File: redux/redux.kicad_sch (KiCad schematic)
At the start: 250 parts, among them J11 DNP, J12 DNP, J13 DNP, J14 Backplane, J3 Common, J4 Ext-2, J5 Ext-1, J6 Master, J7 Ext+1, J8 Ext+2, M1000 Bracket, Q1 MMBT3906, U1 MC100LVEL16, U13 MC100LVEL14, U15 SY89421V, U16 LM311, U34 AD7841, U44 AD586, U45 AD586, U62 LT1086-ADJ, U63 LT1086-ADJ, U64 16715-89002, U65 74CBT3125, U66 SG-615P 19.6608MHz, U67 SN74FB2040, U68 MC100LVEL11, U73 MC100LVEL16, U74 MC10EL34, U75 PCF8584, U76 74ABT540, U79 NEL HS-2810 101MHz

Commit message: redux work
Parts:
- removed J11, J12, J13: DNP, fp:PinHeader_2x10_P2.54mm_Vertical, symbol Connector_Generic:Conn_02x10_Odd_Even
- removed R1, R2, R3, R4, R5, R6, R7, R8: 100, fp:R_Array_Convex_4x0603, symbol Device:R_Pack04
- removed R1038, R1044: DNP, fp:R0805, symbol Device:R_Small
- removed R1040, R1047, R1053, R1054, R1057, R1231, R1232, R1235, R1238, R1241: 31.6, fp:R0805, symbol Device:R_Small
- removed R1242, R1243: 147, fp:R0805, symbol Device:R_Small
- removed RP11: 150, fp:SOIC-16W_5.3x10.2mm_P1.27mm, symbol 16717a:RPack8
- added C2: 1.1n, fp:C0805, symbol Device:C_Small
- added R13, R14: 150, fp:R_Array_Convex_4x0603, symbol Device:R_Pack04
- added R170, R171, R180, R181, R190, R191: 100, fp:SOIC-16W_5.3x10.2mm_P1.27mm, symbol 16717a:RPack8
- R10, R11, R9: value 100 -> 31.6
- R12: value 100 -> 150
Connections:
- net +1.5V: now also R170.10, R170.11, R170.12, R170.13, R170.14, R170.15, R170.16, R170.9, R171.1, R171.2, R171.3, R171.4, R171.5, R171.6, R171.7, R171.8, R180.10, R180.11, R180.12, R180.13, R180.14, R180.15, R180.16, R180.9, R181.1, R181.2, R181.3, R181.4, R181.5, R181.6, R181.7, R181.8, R190.10, R190.11, R190.12, R190.13, R190.14, R190.15, R190.16, R190.9, R191.1, R191.2, R191.3, R191.4, R191.5, R191.6, R191.7, R191.8; no longer R10.1 (R1.1), R10.2 (R2.1), R10.3 (R3.1), R10.4 (R4.1), R11.1 (R1.1), R11.2 (R2.1), R11.3 (R3.1), R11.4 (R4.1), R12.1 (R1.1), R12.2 (R2.1), R12.3 (R3.1), R12.4 (R4.1), R9.1 (R1.1), R9.2 (R2.1), R9.3 (R3.1), R9.4 (R4.1)
- net +3.3VP: now also C2.2
- net -5.2V: now also R12.5 (R4.2), R12.6 (R3.2), R12.7 (R2.2), R12.8 (R1.2), R13.5 (R4.2), R13.6 (R3.2), R13.7 (R2.2), R13.8 (R1.2), R14.5 (R4.2), R14.6 (R3.2), R14.7 (R2.2), R14.8 (R1.2)
- net BA_{0}: now also R191.9
- net BA_{10}: now also R181.11
- net BA_{11}: now also R181.12
- net BA_{12}: now also R181.13
- net BA_{13}: now also R181.14
- net BA_{14}: now also R181.15
- net BA_{15}: now also R181.16
- net BA_{16}: now also R171.9
- net BA_{17}: now also R171.10
- net BA_{18}: now also R171.11
- net BA_{19}: now also R171.12
- net BA_{1}: now also R191.10
- net BA_{20}: now also R171.13
- net BA_{21}: now also R171.14
- net BA_{22}: now also R171.15
- net BA_{23}: now also R171.16
- net BA_{2}: now also R191.11
- net BA_{3}: now also R191.12
- net BA_{4}: now also R191.13
- net BA_{5}: now also R191.14
- net BA_{6}: now also R191.15
- net BA_{7}: now also R191.16
- net BA_{8}: now also R181.9
- net BA_{9}: now also R181.10
- net BB_{0}: now also R190.8; no longer R12.5 (R4.2)
- net BB_{10}: now also R180.6; no longer R10.7 (R2.2)
- net BB_{11}: now also R180.5; no longer R10.8 (R1.2)
- net BB_{12}: now also R180.4; no longer R9.5 (R4.2)
- net BB_{13}: now also R180.3; no longer R9.6 (R3.2)
- net BB_{14}: now also R180.2; no longer R9.7 (R2.2)
- net BB_{15}: now also R180.1; no longer R9.8 (R1.2)
- net BB_{16}: now also R170.8
- net BB_{17}: now also R170.7
- net BB_{18}: now also R170.6
- net BB_{19}: now also R170.5
- net BB_{1}: now also R190.7; no longer R12.6 (R3.2)
- net BB_{20}: now also R170.4
- net BB_{21}: now also R170.3
- net BB_{22}: now also R170.2
- net BB_{23}: now also R170.1
- net BB_{2}: now also R190.6; no longer R12.7 (R2.2)
- net BB_{3}: now also R190.5; no longer R12.8 (R1.2)
- net BB_{4}: now also R190.4; no longer R11.5 (R4.2)
- net BB_{5}: now also R190.3; no longer R11.6 (R3.2)
- net BB_{6}: now also R190.2; no longer R11.7 (R2.2)
- net BB_{7}: now also R190.1; no longer R11.8 (R1.2)
- net BB_{8}: now also R180.8; no longer R10.5 (R4.2)
- net BB_{9}: now also R180.7; no longer R10.6 (R3.2)
- net GND: now also R11.7 (R2.2), R11.8 (R1.2), C2.1
- net TEST_CLK_{L0}: now also R9.6 (R3.2)
- net TEST_CLK_{L1}: now also R9.8 (R1.2)
- net TEST_CLK_{L2}: now also R10.6 (R3.2)
- net TEST_CLK_{L3}: now also R10.8 (R1.2)
- net TEST_CLK_{L4}: now also R11.6 (R3.2)
- net TEST_CLK_{R0}: now also R9.5 (R4.2)
- net TEST_CLK_{R1}: now also R9.7 (R2.2)
- net TEST_CLK_{R2}: now also R10.5 (R4.2)
- net TEST_CLK_{R3}: now also R10.7 (R2.2)
- net TEST_CLK_{R4}: now also R11.5 (R4.2)
- net at U13.3 (OUT_{1}): now also R12.2 (R2.1), R9.1 (R1.1), R9.2 (R2.1)
- net at U13.1 (OUT_{0}): now also R12.4 (R4.1), R9.3 (R3.1), R9.4 (R4.1)
- net at U13.9 (OUT_{4}): now also R11.3 (R3.1), R11.4 (R4.1), R14.4 (R4.1)
- net at U13.5 (OUT_{2}): now also R10.3 (R3.1), R10.4 (R4.1), R13.4 (R4.1)
- net at U13.7 (OUT_{3}): now also R10.1 (R1.1), R10.2 (R2.1), R13.2 (R2.1)
- net at U13.6 (~{OUT_{2}}): now also R13.3 (R3.1)
- net at U13.4 (~{OUT_{1}}): now also R12.1 (R1.1)
- net at U13.2 (~{OUT_{0}}): now also R12.3 (R3.1)
- net at U13.8 (~{OUT_{3}}): now also R13.1 (R1.1)
- net at U13.10 (~{OUT_{4}}): now also R14.3 (R3.1)
- net SYS_CLK renamed SYS_CLK+
- net SYS_CLK_{LEFT} renamed SYS_CLK_{LEFT}+
- net SYS_CLK_{RIGHT} renamed SYS_CLK_{RIGHT}+
- net ~{SYS_CLK_{LEFT}} renamed SYS_CLK_{LEFT}-
- net ~{SYS_CLK_{RIGHT}} renamed SYS_CLK_{RIGHT}-
- net ~{SYS_CLK} renamed SYS_CLK-
- no-connect marks 41 -> 34

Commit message: replace SOIC resistor arrays
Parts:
- removed R213: 51, fp:SOIC-16W_5.3x10.2mm_P1.27mm, symbol 16717a:RPack8
- removed RP10, RP16, RP4, RP5, RP6, RP7, RP8, RP9: 33, fp:SOIC-16W_5.3x10.2mm_P1.27mm, symbol 16717a:RPack8
- removed RP17, RP18: 100, fp:SOIC-16W_5.3x10.2mm_P1.27mm, symbol 16717a:RPack8
- removed RP3: 1k, fp:SOIC-16W_5.3x10.2mm_P1.27mm, symbol 16717a:R_Network15
- added R15, R16, R17: 1k, fp:R_Array_Convex_4x0603, symbol Device:R_Pack04
- added R18, R19, R20, R21, R22, R23, R24, R25, R26, R27, R28, R29, R34, R35, R36, R37: 33, fp:R_Array_Convex_4x0603, symbol Device:R_Pack04
- added R30, R31, R38, R39: 100, fp:R_Array_Convex_4x0603, symbol Device:R_Pack04
- added R32, R33: 51, fp:R_Array_Convex_4x0603, symbol Device:R_Pack04
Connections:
- net +2.5V: now also R38.5 (R4.2), R38.6 (R3.2), R38.7 (R2.2), R38.8 (R1.2), R39.5 (R4.2), R39.6 (R3.2), R39.7 (R2.2), R39.8 (R1.2)
- net +3.3V: now also R15.1 (R1.1), R15.2 (R2.1), R15.3 (R3.1), R15.4 (R4.1), R16.1 (R1.1), R16.2 (R2.1), R16.3 (R3.1), R16.4 (R4.1), R17.1 (R1.1), R17.2 (R2.1), R17.3 (R3.1), R17.4 (R4.1), R30.5 (R4.2), R30.6 (R3.2), R30.7 (R2.2), R30.8 (R1.2), R31.5 (R4.2), R31.6 (R3.2), R31.7 (R2.2), R31.8 (R1.2)
- net CTRL0L: now also R31.1 (R1.1)
- net CTRL0R: now also R30.1 (R1.1)
- net CTRL10L: now also R28.4 (R4.1)
- net CTRL10R: now also R28.3 (R3.1)
- net CTRL1L: now also R31.2 (R2.1)
- net CTRL1R: now also R30.2 (R2.1)
- net CTRL2L: now also R31.3 (R3.1)
- net CTRL2R: now also R30.3 (R3.1)
- net CTRL3L: now also R31.4 (R4.1)
- net CTRL3R: now also R30.4 (R4.1)
- net CTRL6L: now also R29.2 (R2.1)
- net CTRL6R: now also R29.1 (R1.1)
- net CTRL7L: now also R29.4 (R4.1)
- net CTRL7R: now also R29.3 (R3.1)
- net CTRL9L: now also R28.2 (R2.1)
- net CTRL9R: now also R28.1 (R1.1)
- net SYS_CLK+: now also R32.4 (R4.1)
- net SYS_CLK-: now also R32.2 (R2.1)
- net SYS_CLK_{LEFT}+: now also R33.4 (R4.1)
- net SYS_CLK_{LEFT}-: now also R33.2 (R2.1)
- net SYS_CLK_{RIGHT}+: now also R33.3 (R3.1)
- net SYS_CLK_{RIGHT}-: now also R33.1 (R1.1)
- net ZCTRL0: now also R16.8 (R1.2)
- net ZCTRL1: now also R16.7 (R2.2)
- net ZCTRL2: now also R16.6 (R3.2)
- net ZCTRL3: now also R15.6 (R3.2)
- net ZCTRL4: now also R15.8 (R1.2)
- net ZCTRL5: now also R15.7 (R2.2)
- net ZCTRL6: now also R15.5 (R4.2)
- net ~{BIFE_{0}}: now also R38.1 (R1.1)
- net ~{BIFE_{1}}: now also R38.2 (R2.1)
- net ~{BIFE_{2}}: now also R38.3 (R3.1)
- net ~{BIFE_{3}}: now also R38.4 (R4.1)
- net ~{BIFE_{4}}: now also R39.1 (R1.1)
- net ~{BIFE_{5}}: now also R39.2 (R2.1)
- net ~{BIFE_{6}}: now also R39.3 (R3.1)
- net ~{BIFE_{7}}: now also R39.4 (R4.1)
- net ~{EVENT_LEFT_{0}}: now also R36.7 (R2.2)
- net ~{EVENT_LEFT_{1}}: now also R36.5 (R4.2)
- net ~{EVENT_LEFT_{2}}: now also R37.7 (R2.2)
- net ~{EVENT_LEFT_{3}}: now also R37.5 (R4.2)
- net ~{EVENT_LEFT_{4}}: now also R34.7 (R2.2)
- net ~{EVENT_LEFT_{5}}: now also R34.5 (R4.2)
- net ~{EVENT_LEFT_{6}}: now also R35.7 (R2.2)
- net ~{EVENT_LEFT_{7}}: now also R35.5 (R4.2)
- net ~{EVENT_RIGHT_{0}}: now also R36.8 (R1.2)
- net ~{EVENT_RIGHT_{1}}: now also R36.6 (R3.2)
- net ~{EVENT_RIGHT_{2}}: now also R37.8 (R1.2)
- net ~{EVENT_RIGHT_{3}}: now also R37.6 (R3.2)
- net ~{EVENT_RIGHT_{4}}: now also R34.8 (R1.2)
- net ~{EVENT_RIGHT_{5}}: now also R34.6 (R3.2)
- net ~{EVENT_RIGHT_{6}}: now also R35.8 (R1.2)
- net ~{EVENT_RIGHT_{7}}: now also R35.6 (R3.2)
- net ~{MEM_CAS_{L0}}: now also R24.3 (R3.1)
- net ~{MEM_CAS_{L10}}: now also R23.2 (R2.1)
- net ~{MEM_CAS_{L11}}: now also R23.4 (R4.1)
- net ~{MEM_CAS_{L12}}: now also R25.3 (R3.1)
- net ~{MEM_CAS_{L13}}: now also R26.1 (R1.1)
- net ~{MEM_CAS_{L14}}: now also R23.3 (R3.1)
- net ~{MEM_CAS_{L15}}: now also R24.1 (R1.1)
- net ~{MEM_CAS_{L16}}: now also R26.2 (R2.1)
- net ~{MEM_CAS_{L1}}: now also R25.1 (R1.1)
- net ~{MEM_CAS_{L2}}: now also R22.3 (R3.1)
- net ~{MEM_CAS_{L3}}: now also R23.1 (R1.1)
- net ~{MEM_CAS_{L4}}: now also R24.2 (R2.1)
- net ~{MEM_CAS_{L5}}: now also R24.4 (R4.1)
- net ~{MEM_CAS_{L6}}: now also R22.2 (R2.1)
- net ~{MEM_CAS_{L7}}: now also R22.4 (R4.1)
- net ~{MEM_CAS_{L8}}: now also R25.2 (R2.1)
- net ~{MEM_CAS_{L9}}: now also R25.4 (R4.1)
- net ~{MEM_CAS_{R0}}: now also R20.2 (R2.1)
- net ~{MEM_CAS_{R10}}: now also R19.1 (R1.1)
- net ~{MEM_CAS_{R11}}: now also R19.3 (R3.1)
- net ~{MEM_CAS_{R12}}: now also R21.2 (R2.1)
- net ~{MEM_CAS_{R13}}: now also R21.4 (R4.1)
- net ~{MEM_CAS_{R14}}: now also R19.2 (R2.1)
- net ~{MEM_CAS_{R15}}: now also R19.4 (R4.1)
- net ~{MEM_CAS_{R16}}: now also R22.1 (R1.1)
- net ~{MEM_CAS_{R1}}: now also R20.4 (R4.1)
- net ~{MEM_CAS_{R2}}: now also R18.2 (R2.1)
- net ~{MEM_CAS_{R3}}: now also R18.4 (R4.1)
- net ~{MEM_CAS_{R4}}: now also R20.1 (R1.1)
- net ~{MEM_CAS_{R5}}: now also R20.3 (R3.1)
- net ~{MEM_CAS_{R6}}: now also R18.1 (R1.1)
- net ~{MEM_CAS_{R7}}: now also R18.3 (R3.1)
- net ~{MEM_CAS_{R8}}: now also R21.1 (R1.1)
- net ~{MEM_CAS_{R9}}: now also R21.3 (R3.1)
- net ~{ZCS_{0}}: now also R16.5 (R4.2), R26.3 (R3.1)
- net ~{ZCS_{1}}: now also R17.8 (R1.2), R26.4 (R4.1)
- net ~{ZCS_{2}}: now also R17.7 (R2.2), R27.1 (R1.1)
- net ~{ZCS_{3}}: now also R17.6 (R3.2), R27.2 (R2.1)
- net ~{ZCS_{4}}: now also R17.5 (R4.2), R27.3 (R3.1)
- net at C1124.1, R1119.1: now also R33.7 (R2.2), R33.8 (R1.2)
- net at U64.118 (~{ZCS_{4}}): now also R27.6 (R3.2)
- net at U64.117 (~{ZCS_{3}}): now also R27.7 (R2.2)
- net at U64.116 (~{ZCS_{2}}): now also R27.8 (R1.2)
- net at U64.115 (~{ZCS_{1}}): now also R26.5 (R4.2)
- net at U64.114 (~{ZCS_{0}}): now also R26.6 (R3.2)
- net at U64.102 (~{MEM_CAS_{L16}}): now also R26.7 (R2.2)
- net at U64.101 (~{MEM_CAS_{L13}}): now also R26.8 (R1.2)
- net at R1116.2, U68.1 (Y_{0}): now also R32.7 (R2.2)
- net at U64.100 (~{MEM_CAS_{L9}}): now also R25.5 (R4.2)
- net at U64.135 (CTRL9): now also R28.7 (R2.2), R28.8 (R1.2)
- net at U64.137 (CTRL10R): now also R28.6 (R3.2)
- net at U64.138 (CTRL10L): now also R28.5 (R4.2)
- net at U64.140 (CTRL6R): now also R29.8 (R1.2)
- net at U64.141 (CTRL6L): now also R29.7 (R2.2)
- net at U64.142 (CTRL7R): now also R29.6 (R3.2)
- net at U64.143 (CTRL7L): now also R29.5 (R4.2)
- net at U64.65 (~{MEM_CAS_{R6}}): now also R18.8 (R1.2)
- net at U64.66 (~{MEM_CAS_{R2}}): now also R18.7 (R2.2)
- net at U64.67 (~{MEM_CAS_{R7}}): now also R18.6 (R3.2)
- net at U64.68 (~{MEM_CAS_{R3}}): now also R18.5 (R4.2)
- net at U64.69 (~{MEM_CAS_{R10}}): now also R19.8 (R1.2)
- net at U64.70 (~{MEM_CAS_{R14}}): now also R19.7 (R2.2)
- net at U64.71 (~{MEM_CAS_{R11}}): now also R19.6 (R3.2)
- net at U64.72 (~{MEM_CAS_{R15}}): now also R19.5 (R4.2)
- net at U64.73 (~{MEM_CAS_{R4}}): now also R20.8 (R1.2)
- net at U64.74 (~{MEM_CAS_{R0}}): now also R20.7 (R2.2)
- net at U64.75 (~{MEM_CAS_{R5}}): now also R20.6 (R3.2)
- net at U64.76 (~{MEM_CAS_{R1}}): now also R20.5 (R4.2)
- net at U64.77 (~{MEM_CAS_{R8}}): now also R21.8 (R1.2)
- net at U64.81 (~{MEM_CAS_{R12}}): now also R21.7 (R2.2)
- net at U64.82 (~{MEM_CAS_{R9}}): now also R21.6 (R3.2)
- net at U64.83 (~{MEM_CAS_{R13}}): now also R21.5 (R4.2)
- net at U64.84 (~{MEM_CAS_{R16}}): now also R22.8 (R1.2)
- net at U64.85 (~{MEM_CAS_{L6}}): now also R22.7 (R2.2)
- net at U64.86 (~{MEM_CAS_{L2}}): now also R22.6 (R3.2)
- net at U64.87 (~{MEM_CAS_{L7}}): now also R22.5 (R4.2)
- net at U64.88 (~{MEM_CAS_{L3}}): now also R23.8 (R1.2)
- net at U64.89 (~{MEM_CAS_{L10}}): now also R23.7 (R2.2)
- net at U64.90 (~{MEM_CAS_{L14}}): now also R23.6 (R3.2)
- net at U64.91 (~{MEM_CAS_{L11}}): now also R23.5 (R4.2)
- net at U64.92 (~{MEM_CAS_{L15}}): now also R24.8 (R1.2)
- net at U64.93 (~{MEM_CAS_{L4}}): now also R24.7 (R2.2)
- net at U64.94 (~{MEM_CAS_{L0}}): now also R24.6 (R3.2)
- net at U64.95 (~{MEM_CAS_{L5}}): now also R24.5 (R4.2)
- net at U64.96 (~{MEM_CAS_{L1}}): now also R25.8 (R1.2)
- net at U64.97 (~{MEM_CAS_{L8}}): now also R25.7 (R2.2)
- net at U64.99 (~{MEM_CAS_{L12}}): now also R25.6 (R3.2)
- net at U76.18 (Y0): now also R36.1 (R1.1), R36.2 (R2.1)
- net at U76.17 (Y1): now also R36.3 (R3.1), R36.4 (R4.1)
- net at U76.16 (Y2): now also R37.1 (R1.1), R37.2 (R2.1)
- net at U76.15 (Y3): now also R37.3 (R3.1), R37.4 (R4.1)
- net at U76.14 (Y4): now also R34.1 (R1.1), R34.2 (R2.1)
- net at U76.13 (Y5): now also R34.3 (R3.1), R34.4 (R4.1)
- net at U76.12 (Y6): now also R35.1 (R1.1), R35.2 (R2.1)
- net at U76.11 (Y7): now also R35.3 (R3.1), R35.4 (R4.1)
- net at R1115.2, U68.2 (~{Y_{0}}): now also R32.5 (R4.2)
- net at C1123.2, R1118.1: now also R33.5 (R4.2), R33.6 (R3.2)
- no-connect marks 34 -> 31
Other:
- moved on the sheet: C1127, C1129, C1134

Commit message: Rework acquisition ASIC routing
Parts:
- removed C176: DNP, fp:C_Axial_P38.1mm, symbol Device:C_Polarized
- removed R1039, R1045, R1046, R1052: 100, fp:R0805, symbol Device:R_Small
- removed R1142, R1149, R1150, R1151: 51, fp:R0603, symbol Device:R_Small
- removed R170, R171, R180, R181, R190, R191: 100, fp:SOIC-16W_5.3x10.2mm_P1.27mm, symbol 16717a:RPack8
- removed RP12, RP13: 51, fp:SOIC-16W_5.3x10.2mm_P1.27mm, symbol 16717a:RPack8
- added C3, C4, C5, C6, C7, C8: 51n, fp:C0805, symbol Device:C_Small
- added R40, R41, R42, R43, R44, R45, R46, R47, R48, R49, R50, R51, R56: 100, fp:R_Array_Convex_4x0603, symbol Device:R_Pack04
- added R52, R53, R54, R55, R58: 51, fp:R_Array_Convex_4x0603, symbol Device:R_Pack04
- added R57: 0, fp:R0805, symbol Device:R_Small
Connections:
- net +1.5V: now also C3.2, C4.1, C5.2, C6.1, C7.2, C8.1, R40.5 (R4.2), R40.6 (R3.2), R40.7 (R2.2), R40.8 (R1.2), R41.5 (R4.2), R41.6 (R3.2), R41.7 (R2.2), R41.8 (R1.2), R42.5 (R4.2), R42.6 (R3.2), R42.7 (R2.2), R42.8 (R1.2), R43.5 (R4.2), R43.6 (R3.2), R43.7 (R2.2), R43.8 (R1.2), R44.5 (R4.2), R44.6 (R3.2), R44.7 (R2.2), R44.8 (R1.2), R45.5 (R4.2), R45.6 (R3.2), R45.7 (R2.2), R45.8 (R1.2), R46.5 (R4.2), R46.6 (R3.2), R46.7 (R2.2), R46.8 (R1.2), R47.5 (R4.2), R47.6 (R3.2), R47.7 (R2.2), R47.8 (R1.2), R48.5 (R4.2), R48.6 (R3.2), R48.7 (R2.2), R48.8 (R1.2), R49.5 (R4.2), R49.6 (R3.2), R49.7 (R2.2), R49.8 (R1.2), R50.5 (R4.2), R50.6 (R3.2), R50.7 (R2.2), R50.8 (R1.2), R51.5 (R4.2), R51.6 (R3.2), R51.7 (R2.2), R51.8 (R1.2), R52.1 (R1.1), R52.2 (R2.1), R52.3 (R3.1), R52.4 (R4.1), R53.2 (R2.1), R53.3 (R3.1), R53.4 (R4.1), R54.1 (R1.1), R54.2 (R2.1), R54.3 (R3.1), R55.1 (R1.1), R55.2 (R2.1), R55.3 (R3.1), R55.4 (R4.1)
- net +5V: now also R57.2; no longer C1112.1, U63.3 (VI)
- net -3.3V: now also R56.5 (R4.2), R56.6 (R3.2), R56.7 (R2.2), R56.8 (R1.2)
- net BA_{0}: now also R45.4 (R4.1)
- net BA_{10}: now also R41.2 (R2.1)
- net BA_{11}: now also R41.1 (R1.1)
- net BA_{12}: now also R40.4 (R4.1)
- net BA_{13}: now also R40.3 (R3.1)
- net BA_{14}: now also R40.2 (R2.1)
- net BA_{15}: now also R40.1 (R1.1)
- net BA_{16}: now also R43.4 (R4.1)
- net BA_{17}: now also R43.3 (R3.1)
- net BA_{18}: now also R43.2 (R2.1)
- net BA_{19}: now also R43.1 (R1.1)
- net BA_{1}: now also R45.3 (R3.1)
- net BA_{20}: now also R42.4 (R4.1)
- net BA_{21}: now also R42.3 (R3.1)
- net BA_{22}: now also R42.2 (R2.1)
- net BA_{23}: now also R42.1 (R1.1)
- net BA_{2}: now also R45.2 (R2.1)
- net BA_{3}: now also R45.1 (R1.1)
- net BA_{4}: now also R44.4 (R4.1)
- net BA_{5}: now also R44.3 (R3.1)
- net BA_{6}: now also R44.2 (R2.1)
- net BA_{7}: now also R44.1 (R1.1)
- net BA_{8}: now also R41.4 (R4.1)
- net BA_{9}: now also R41.3 (R3.1)
- net BB_{0}: now also R46.1 (R1.1)
- net BB_{10}: now also R49.3 (R3.1)
- net BB_{11}: now also R49.4 (R4.1)
- net BB_{12}: now also R48.1 (R1.1)
- net BB_{13}: now also R48.2 (R2.1)
- net BB_{14}: now also R48.3 (R3.1)
- net BB_{15}: now also R48.4 (R4.1)
- net BB_{16}: now also R51.1 (R1.1)
- net BB_{17}: now also R51.2 (R2.1)
- net BB_{18}: now also R51.3 (R3.1)
- net BB_{19}: now also R51.4 (R4.1)
- net BB_{1}: now also R46.2 (R2.1)
- net BB_{20}: now also R50.1 (R1.1)
- net BB_{21}: now also R50.2 (R2.1)
- net BB_{22}: now also R50.3 (R3.1)
- net BB_{23}: now also R50.4 (R4.1)
- net BB_{2}: now also R46.3 (R3.1)
- net BB_{3}: now also R46.4 (R4.1)
- net BB_{4}: now also R47.1 (R1.1)
- net BB_{5}: now also R47.2 (R2.1)
- net BB_{6}: now also R47.3 (R3.1)
- net BB_{7}: now also R47.4 (R4.1)
- net BB_{8}: now also R49.1 (R1.1)
- net BB_{9}: now also R49.2 (R2.1)
- net DX0: now also R53.6 (R3.2), R54.7 (R2.2)
- net DX1: now also R53.5 (R4.2), R54.8 (R1.2)
- net DX2: now also R52.8 (R1.2), R55.5 (R4.2)
- net DX3: now also R52.7 (R2.2), R55.6 (R3.2)
- net DX4: now also R52.6 (R3.2), R55.7 (R2.2)
- net DX5: now also R52.5 (R4.2), R55.8 (R1.2)
- net GND: now also C1119.2, C1120.2, C3.1, C4.2, C5.1, C6.2, C7.1, C8.2
- net Left Acquisition/N5/N25: now also R53.7 (R2.2), R53.8 (R1.2)
- net Right Acquisition/N5/N25: now also R54.5 (R4.2), R54.6 (R3.2)
- net ~{MEM_RAS_{LL}}: now also R58.3 (R3.1)
- net ~{MEM_RAS_{LU}}: now also R58.4 (R4.1)
- net ~{MEM_RAS_{RL}}: now also R58.1 (R1.1)
- net ~{MEM_RAS_{RU}}: now also R58.2 (R2.1)
- net at U13.16 (SCLK), U74.1 (CLK/2): now also R56.1 (R1.1)
- net at U74.2 (~{CLK/2}): now also R56.4 (R4.1)
- net at U13.14 (~{CLK}), U74.4 (CLK/4): now also R56.3 (R3.1)
- net at U13.15 (CLK), U74.5 (~{CLK/4}): now also R56.2 (R2.1)
- net at U64.58 (~{MEM_RAS_{LU}}): now also R58.5 (R4.2)
- net at U64.59 (~{MEM_RAS_{LL}}): now also R58.6 (R3.2)
- net at U64.61 (~{MEM_RAS_{RU}}): now also R58.7 (R2.2)
- net at U64.62 (~{MEM_RAS_{RL}}): now also R58.8 (R1.2)
- net at R1166.1: now also R54.4 (R4.1)
- net at R1165.1: now also R53.1 (R1.1)
- new net: C1112.1, R57.1, U63.3 (VI)
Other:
- moved on the sheet: C1197, C1198, R1165, R1166

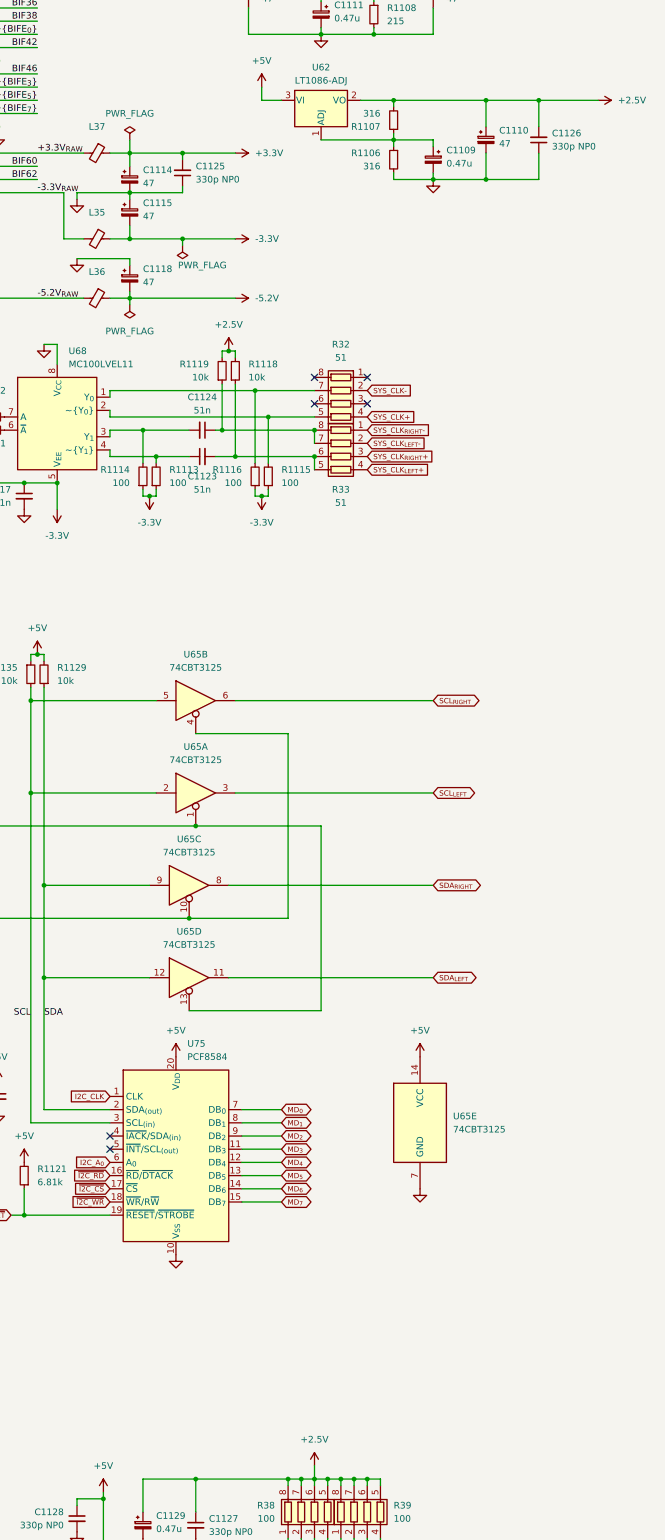
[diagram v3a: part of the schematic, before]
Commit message: length matching & rounded tracks
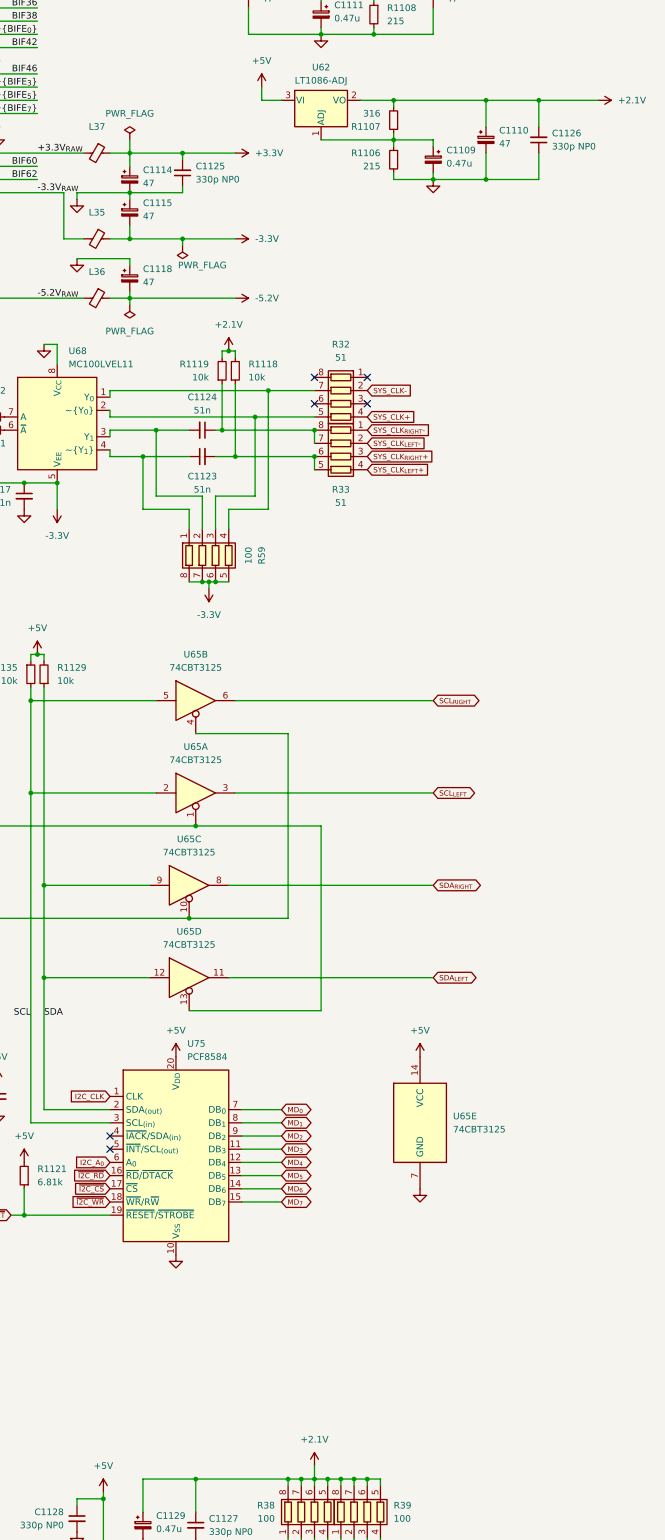
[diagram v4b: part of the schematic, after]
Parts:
- removed R1113, R1114, R1115, R1116: 100, fp:R0805, symbol Device:R_Small
- added R59: 100, fp:R_Array_Convex_4x0603, symbol Device:R_Pack04
- R1106: value 316 -> 215
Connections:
- net -3.3V: now also R59.5 (R4.2), R59.6 (R3.2), R59.7 (R2.2), R59.8 (R1.2)
- net at R32.5 (R4.2), U68.2 (~{Y_{0}}): now also R59.3 (R3.1)
- net at R32.7 (R2.2), U68.1 (Y_{0}): now also R59.4 (R4.1)
- net at C1123.1, U68.4 (~{Y_{1}}): now also R59.1 (R1.1)
- net at C1124.2, U68.3 (Y_{1}): now also R59.2 (R2.1)
- net +2.5V renamed +2.1V
